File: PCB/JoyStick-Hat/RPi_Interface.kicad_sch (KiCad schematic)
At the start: 0 parts

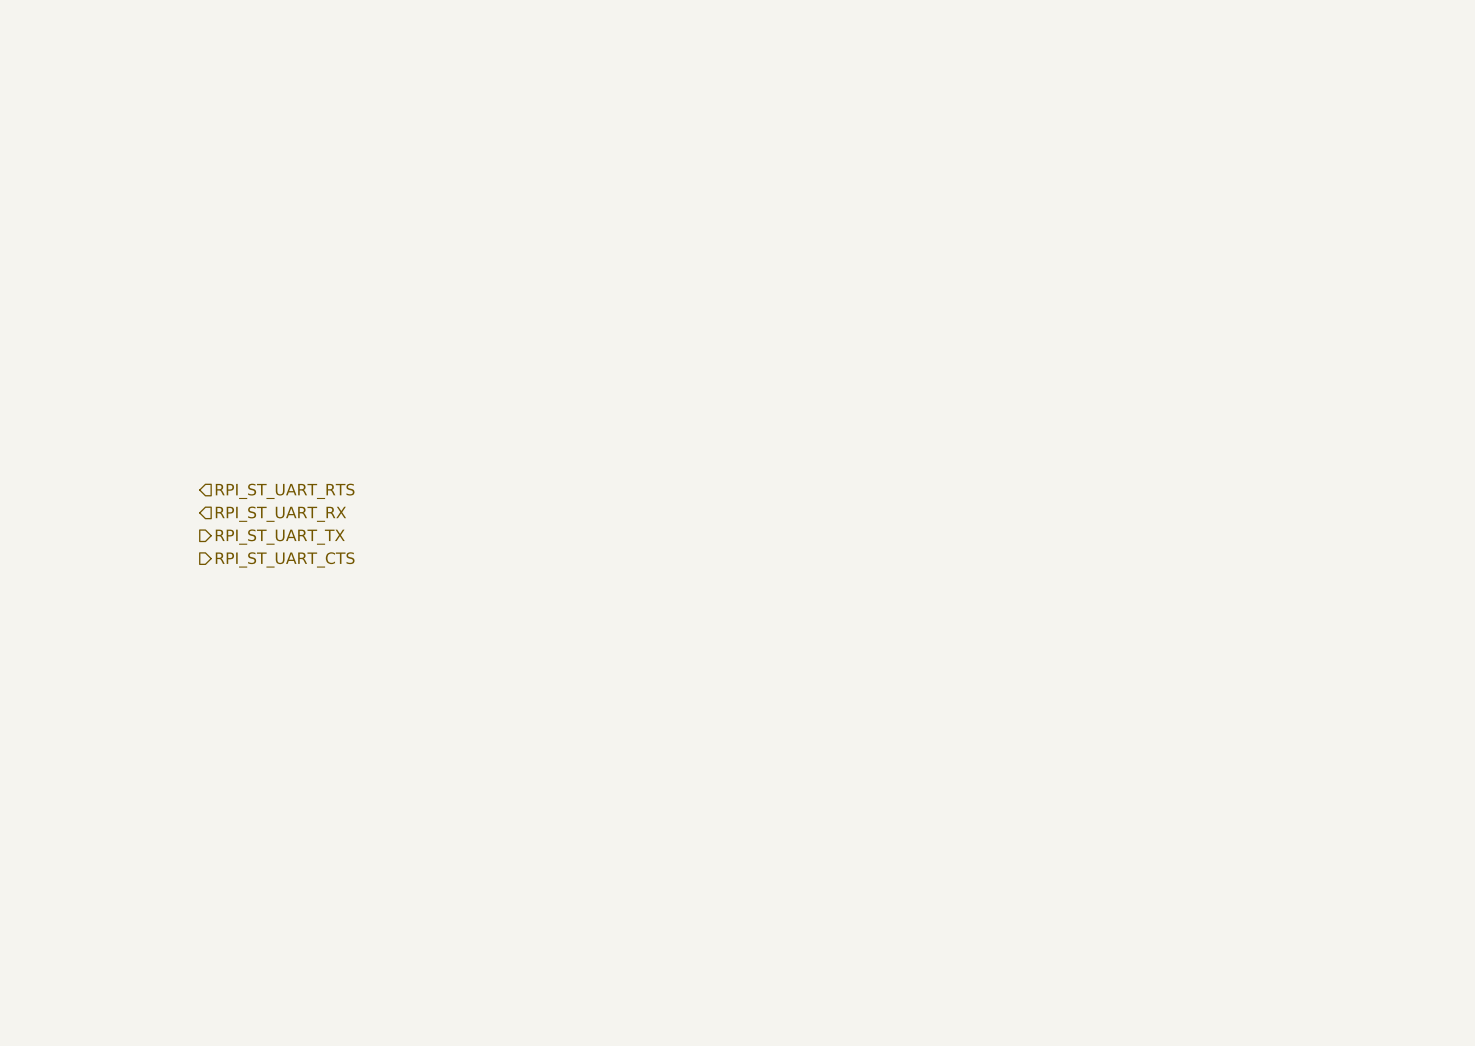
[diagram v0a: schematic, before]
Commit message: LED drivers and Joystick
Finished LED driver scheamtics, corrected some problems with symbols. added conenctors for joystick and buttons, connected RPI pins to MCU
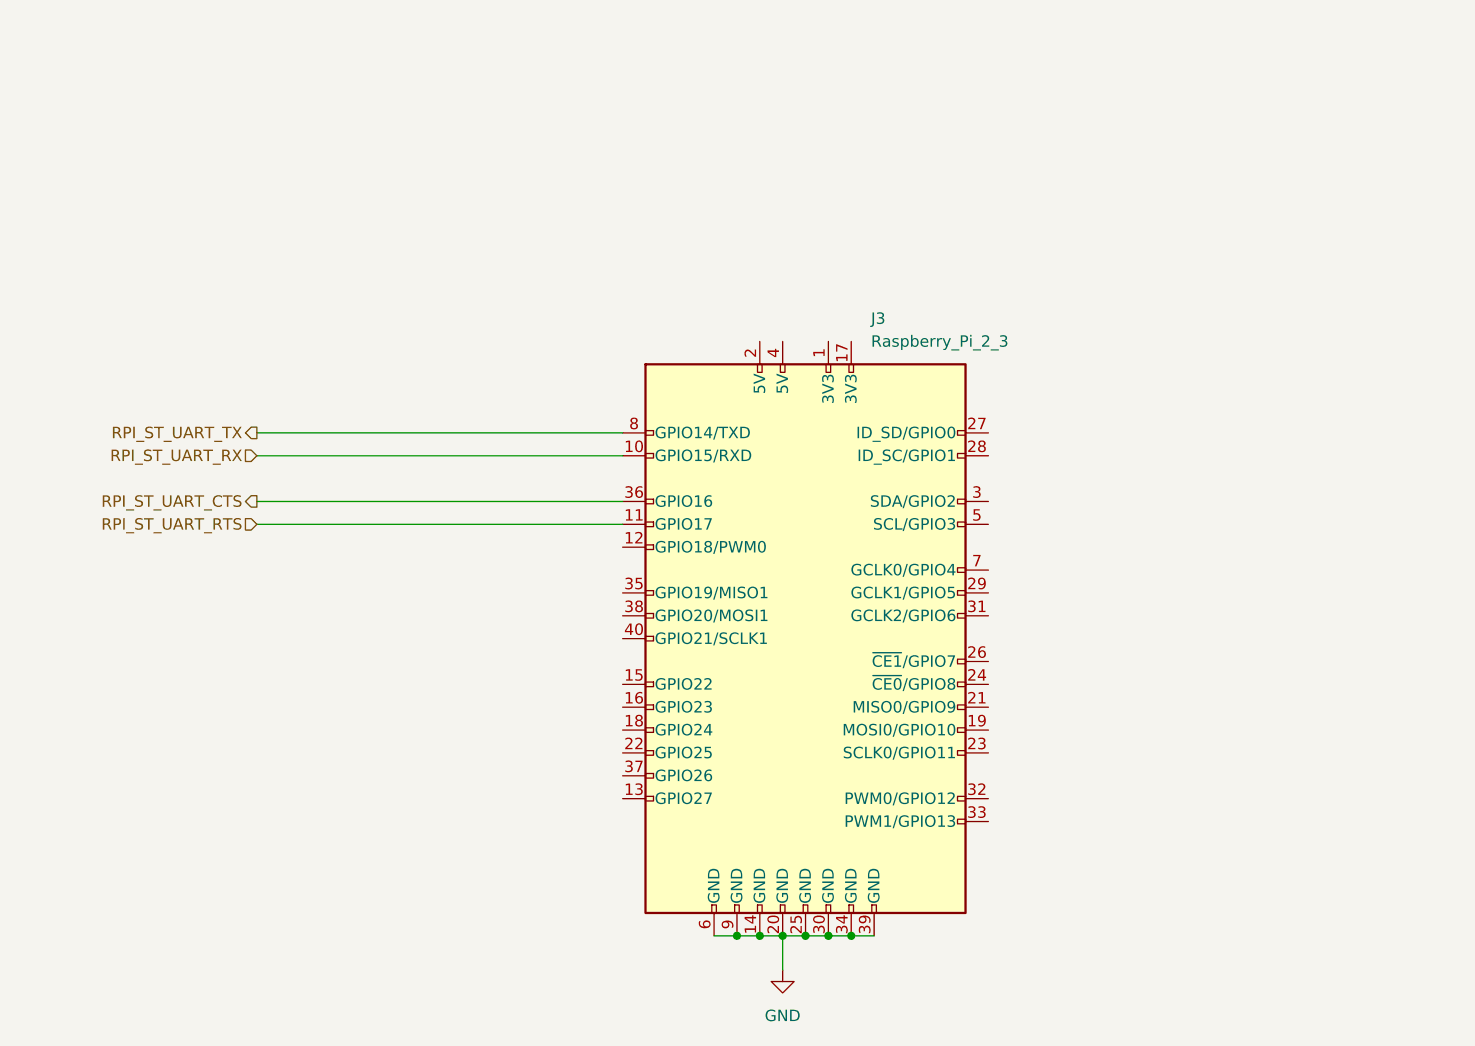
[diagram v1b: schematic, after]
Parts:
- added J3: Raspberry_Pi_2_3, symbol Connector:Raspberry_Pi_2_3
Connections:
- net RPI_ST_UART_CTS: now also J3.36 (GPIO16)
- net RPI_ST_UART_RTS: now also J3.11 (GPIO17)
- net RPI_ST_UART_RX: now also J3.10 (GPIO15/RXD)
- net RPI_ST_UART_TX: now also J3.8 (GPIO14/TXD)
- new net GND: J3.14 (GND), J3.20 (GND), J3.25 (GND), J3.30 (GND), J3.34 (GND), J3.39 (GND), J3.6 (GND), J3.9 (GND)
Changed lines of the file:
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@@
 (kicad_sch (version 20230121) (generator eeschema)
   (paper "A4")
-  (hierarchical_label "RPI_ST_UART_RX" (shape input) (at 106.68 72.39 0) (fields_autoplaced)
-    (effects (font (size 1.27 1.27)) (justify left))
+  (junction (at 179.07 119.38) (diameter 0) (color 0 0 0 0)
   )
-  (hierarchical_label "RPI_ST_UART_CTS" (shape output) (at 106.68 77.47 0) (fields_autoplaced)
-    (effects (font (size 1.27 1.27)) (justify left))
+  (junction (at 176.53 119.38) (diameter 0) (color 0 0 0 0)
   )
-  (hierarchical_label "RPI_ST_UART_RTS" (shape input) (at 106.68 69.85 0) (fields_autoplaced)
-    (effects (font (size 1.27 1.27)) (justify left))
+  (junction (at 168.91 119.38) (diameter 0) (color 0 0 0 0)
   )
-  (hierarchical_label "RPI_ST_UART_TX" (shape output) (at 106.68 74.93 0) (fields_autoplaced)
-    (effects (font (size 1.27 1.27)) (justify left))
+  (junction (at 171.45 119.38) (diameter 0) (color 0 0 0 0)
+  )
+  (junction (at 173.99 119.38) (diameter 0) (color 0 0 0 0)
+  )
+  (junction (at 166.37 119.38) (diameter 0) (color 0 0 0 0)
+  )
+  (wire (pts (xy 113.03 71.12) (xy 153.67 71.12))
+    (stroke (width 0) (type default))
+  )
+  (wire (pts (xy 171.45 119.38) (xy 171.45 123.19))
+    (stroke (width 0) (type default))
+  )
+  (wire (pts (xy 113.03 63.5) (xy 153.67 63.5))
+    (stroke (width 0) (type default))
+  )
+  (wire (pts (xy 163.83 119.38) (xy 166.37 119.38))
+    (stroke (width 0) (type default))
+  )
+  (wire (pts (xy 113.03 66.04) (xy 153.67 66.04))
+    (stroke (width 0) (type default))
+  )
+  (wire (pts (xy 113.03 73.66) (xy 153.67 73.66))
+    (stroke (width 0) (type default))
+  )
+  (wire (pts (xy 173.99 119.38) (xy 176.53 119.38))
+    (stroke (width 0) (type default))
+  )
+  (wire (pts (xy 176.53 119.38) (xy 179.07 119.38))
+    (stroke (width 0) (type default))
+  )
+  (wire (pts (xy 168.91 119.38) (xy 171.45 119.38))
+    (stroke (width 0) (type default))
+  )
+  (wire (pts (xy 166.37 119.38) (xy 168.91 119.38))
+    (stroke (width 0) (type default))
+  )
+  (wire (pts (xy 171.45 119.38) (xy 173.99 119.38))
+    (stroke (width 0) (type default))
+  )
+  (wire (pts (xy 179.07 119.38) (xy 181.61 119.38))
+    (stroke (width 0) (type default))
+  )
+  (hierarchical_label "RPI_ST_UART_RX" (shape input) (at 113.03 66.04 180) (fields_autoplaced)
+    (effects (font (size 1.27 1.27)) (justify right))
+  )
+  (hierarchical_label "RPI_ST_UART_CTS" (shape output) (at 113.03 71.12 180) (fields_autoplaced)
+    (effects (font (size 1.27 1.27)) (justify right))
+  )
+  (hierarchical_label "RPI_ST_UART_RTS" (shape input) (at 113.03 73.66 180) (fields_autoplaced)
+    (effects (font (size 1.27 1.27)) (justify right))
+  )
+  (hierarchical_label "RPI_ST_UART_TX" (shape output) (at 113.03 63.5 180) (fields_autoplaced)
+    (effects (font (size 1.27 1.27)) (justify right))
+  )
+  (symbol (lib_id "Connector:Raspberry_Pi_2_3") (at 173.99 86.36 0) (unit 1)
+    (in_bom yes) (on_board yes) (dnp no) (fields_autoplaced)
+    (property "Reference" "J3" (at 181.2641 50.8 0)
+      (effects (font (size 1.27 1.27)) (justify left))
+    )
+    (property "Value" "Raspberry_Pi_2_3" (at 181.2641 53.34 0)
+      (effects (font (size 1.27 1.27)) (justify left))
+    )
+    (property "Footprint" "" (at 173.99 86.36 0)
+      (effects (font (size 1.27 1.27)) hide)
+    )
+    (property "Datasheet" "https://www.raspberrypi.org/documentation/hardware/raspberrypi/schematics/rpi_SCH_3bplus_1p0_reduced.pdf" (at 173.99 86.36 0)
+      (effects (font (size 1.27 1.27)) hide)
+    )
+    (pin "1")
+    (pin "10")
+    (pin "11")
+    (pin "12")
+    (pin "13")
+    (pin "14")
+    (pin "15")
+    (pin "16")
+    (pin "17")
+    (pin "18")
+    (pin "19")
+    (pin "2")
+    (pin "20")
+    (pin "21")
+    (pin "22")
+    (pin "23")
+    (pin "24")
+    (pin "25")
+    (pin "26")
+    (pin "27")
+    (pin "28")
+    (pin "29")
+    (pin "3")
+    (pin "30")
+    (pin "31")
+    (pin "32")
+    (pin "33")
+    (pin "34")
+    (pin "35")
+    (pin "36")
+    (pin "37")
+    (pin "38")
+    (pin "39")
+    (pin "4")
+    (pin "40")
+    (pin "5")
+    (pin "6")
+    (pin "7")
+    (pin "8")
+    (pin "9")
+    (instances
+      (project "JoyStick-Hat"
+        (path "/cf0c81b5-5bdf-47c3-83c0-f6980f515e65/8b1a07d6-2313-4cc6-a8d0-b86e58239c25"
+          (reference "J3") (unit 1)
+        )
+      )
+    )
+  )
+  (symbol (lib_id "power:GND") (at 171.45 123.19 0) (unit 1)
+    (in_bom yes) (on_board yes) (dnp no) (fields_autoplaced)
+    (property "Reference" "#PWR038" (at 171.45 129.54 0)
+      (effects (font (size 1.27 1.27)) hide)
+    )
+    (property "Value" "GND" (at 171.45 128.27 0)
+      (effects (font (size 1.27 1.27)))
+    )
+    (property "Footprint" "" (at 171.45 123.19 0)
+      (effects (font (size 1.27 1.27)) hide)
+    )
+    (property "Datasheet" "" (at 171.45 123.19 0)
+      (effects (font (size 1.27 1.27)) hide)
+    )
+    (pin "1")
+    (instances
+      (project "JoyStick-Hat"
+        (path "/cf0c81b5-5bdf-47c3-83c0-f6980f515e65/8b1a07d6-2313-4cc6-a8d0-b86e58239c25"
+          (reference "#PWR038") (unit 1)
+        )
+      )
+    )
   )
 )

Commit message: Schematic Complete
Schematic completed. Moved to 100 pin version of STM32 MCU for more connectivity and better muxing of internal peripherals with pins.
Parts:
- added C24, C25: UCM1C470MCL1GS, AVR-KiCAD-Lib-Capacitors:UCM1C470MCL1GS, symbol AVR-KiCAD-Lib-Capacitors:UCM1C470MCL1GS
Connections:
- net GND: now also C24.2, C25.2
- net +5V: now reaches J3.2 (5V)
- net +5V: now also J3.4 (5V), C24.1, C25.1

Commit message: PCB Created
Schematic and footprint bugs knocked out PCB created and parts imported into board.
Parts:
- J3: footprint (none) -> Connector_PinHeader_2.54mm:PinHeader_2x21_P2.54mm_Vertical
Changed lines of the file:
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@@
       (effects (font (size 1.27 1.27)) (justify left))
     )
-    (property "Footprint" "" (at 173.99 86.36 0)
+    (property "Footprint" "Connector_PinHeader_2.54mm:PinHeader_2x21_P2.54mm_Vertical" (at 173.99 86.36 0)
       (effects (font (size 1.27 1.27)) hide)
     )

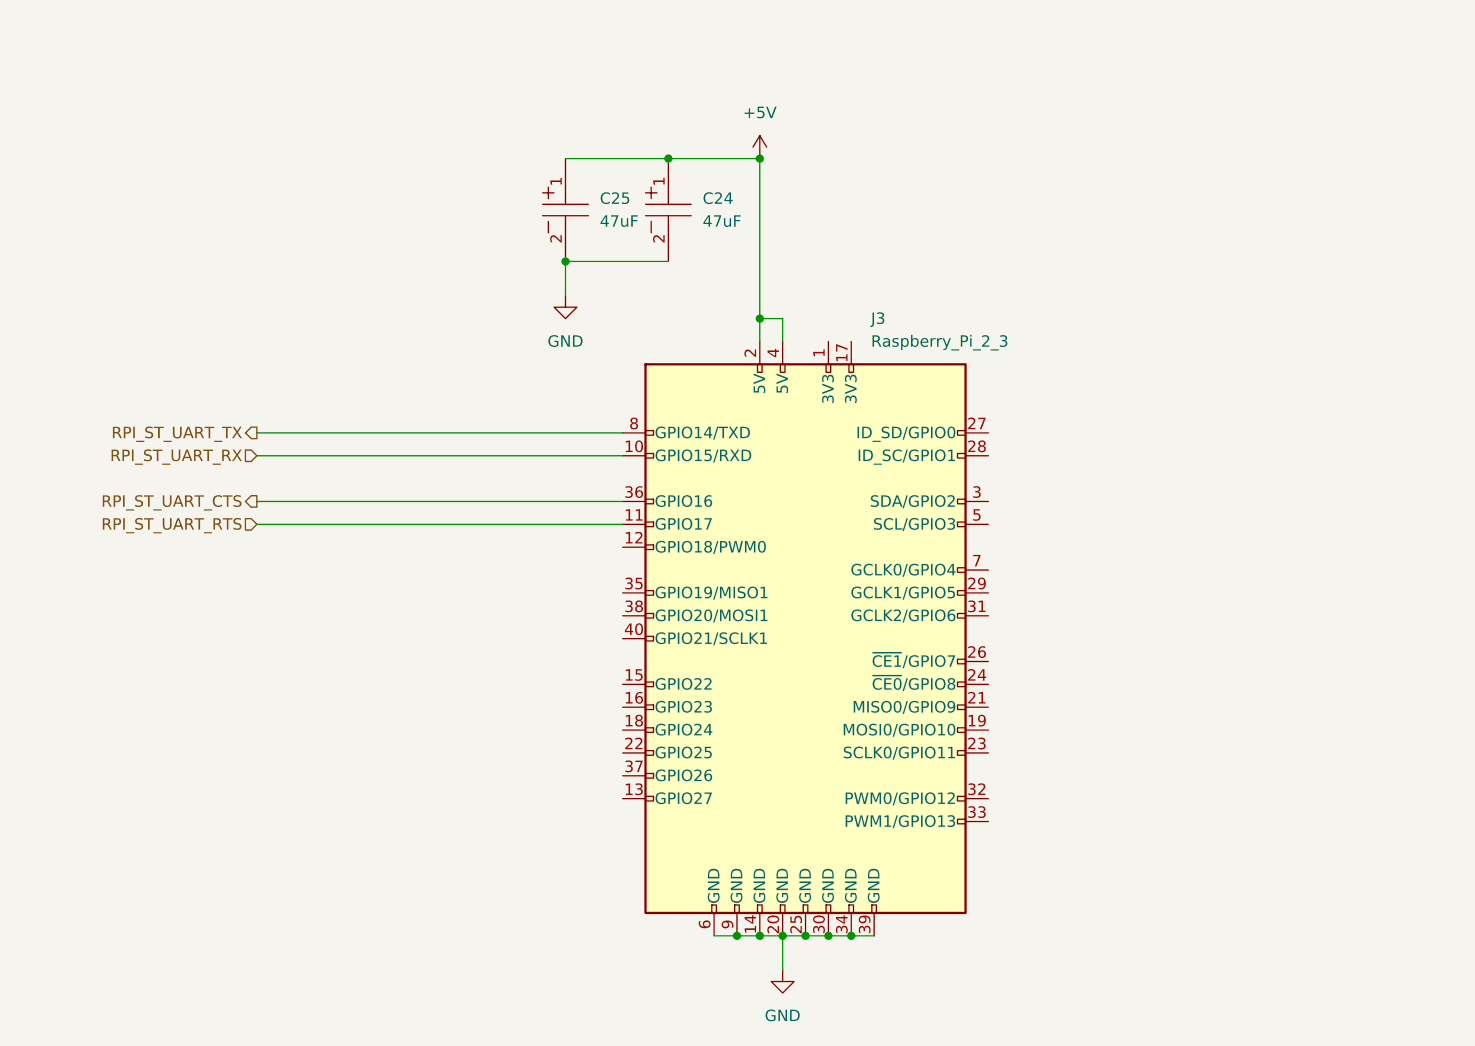
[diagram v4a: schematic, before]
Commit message: LEDs and Additional connectors
Added heartbeat and diagnostic LEDs to STM32 and RPi3 schematics so we can directly flash them for debug purposes. Added a connector for serial port diagnostics on STM32. Added rotary switch interface for STM32 and added pullups to button connectors.
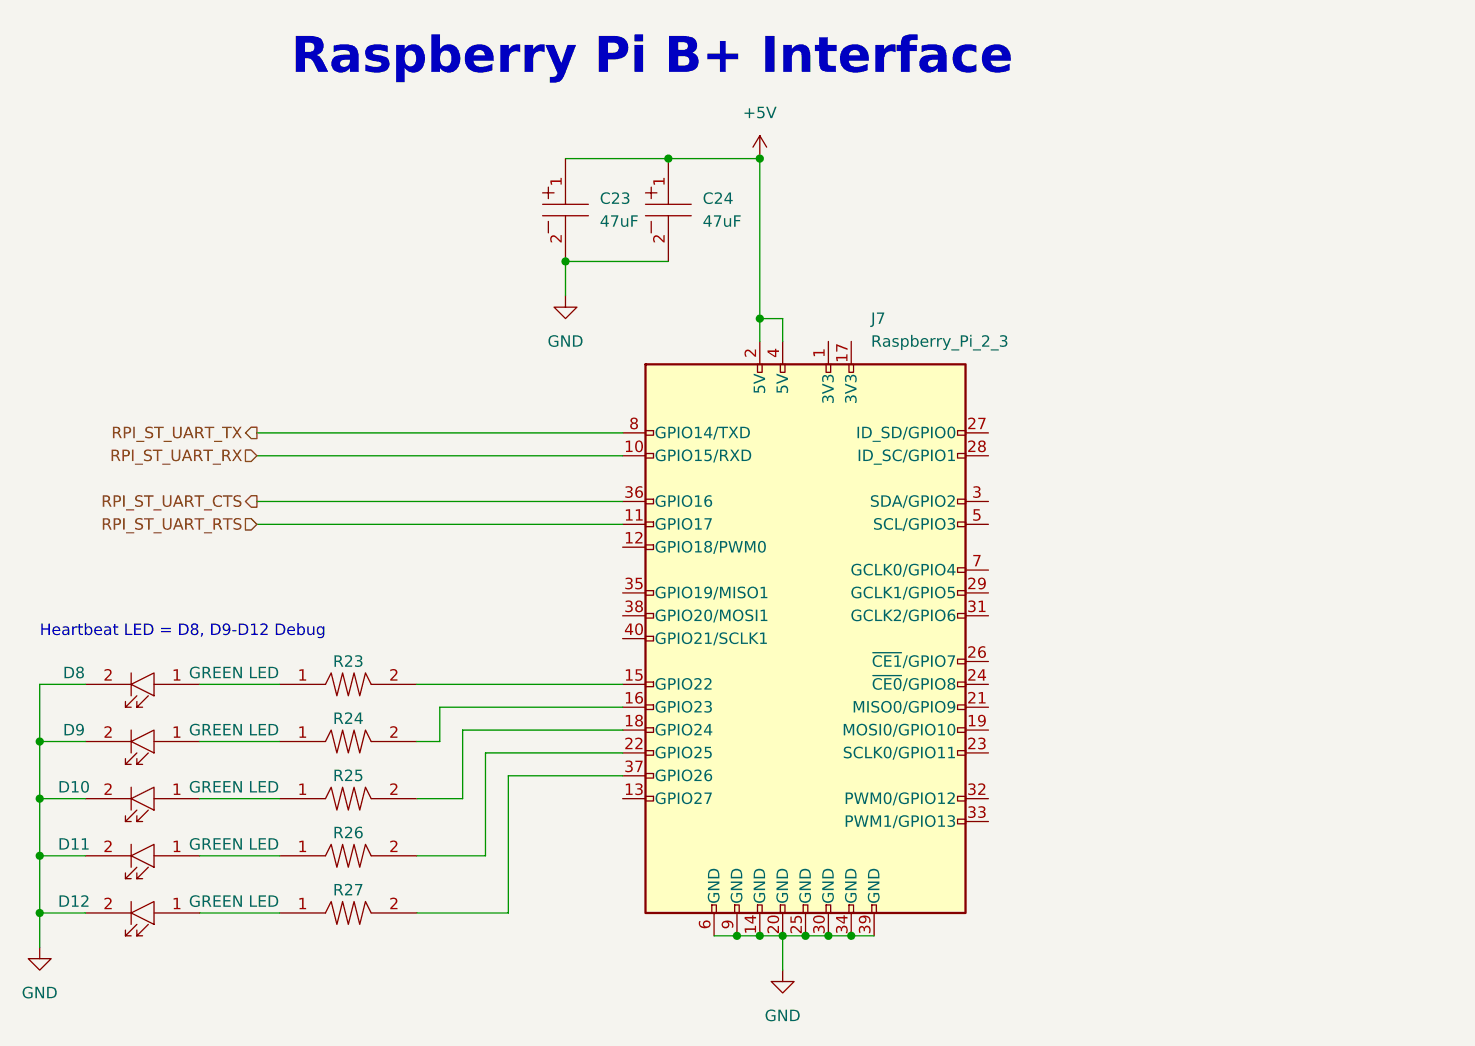
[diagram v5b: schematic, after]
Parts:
- added D10, D11, D12, D8, D9: LTST-C194KGKT, AVR-KiCAD-Lib-Diodes:LED0603, symbol AVR-KiCAD-Lib-Diodes:LTST-C194KGKT
- added R23, R24, R25, R26, R27: RC0603FR-07470RL, AVR-KiCAD-Lib-Resistors:R0603, symbol AVR-KiCAD-Lib-Resistors:RC0603FR-07470RL
- renumbered C25 to C23, J3 to J7
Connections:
- net GND: now also D10.2, D11.2, D12.2, D8.2, D9.2
- net at J7.15 (GPIO22): now also R23.2
- net at J7.16 (GPIO23): now also R24.2
- net at J7.18 (GPIO24): now also R25.2
- net at J7.22 (GPIO25): now also R26.2
- net at J7.37 (GPIO26): now also R27.2
- new net: D12.1, R27.1
- new net: D8.1, R23.1
- new net: D11.1, R26.1
- new net: D9.1, R24.1
- new net: D10.1, R25.1
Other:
- note added: "Heartbeat LED = D8, D9-D12 Debug"
- note added: "Raspberry Pi B+ Interface"

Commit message: Board Tweaks and progress
Made progress with baord. Adjusted the position of RPi header to be correct and absolute. Changed location of regulator modules and power input capacitors. Added 3D models missing from the larger components. Changed connectors and positions for just about everything. Added connnector for LED driver duagher board .
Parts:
- J7: footprint Connector_PinHeader_2.54mm:PinHeader_2x21_P2.54mm_Vertical -> AVR-KiCAD-Lib-Connectors:PinHeader_2x21_P2.54mm_Vertical
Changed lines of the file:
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@@
       (effects (font (size 1.27 1.27)) (justify left))
     )
-    (property "Footprint" "Connector_PinHeader_2.54mm:PinHeader_2x21_P2.54mm_Vertical" (at 173.99 86.36 0)
+    (property "Footprint" "AVR-KiCAD-Lib-Connectors:PinHeader_2x21_P2.54mm_Vertical" (at 173.99 86.36 0)
       (effects (font (size 1.27 1.27)) hide)
     )
